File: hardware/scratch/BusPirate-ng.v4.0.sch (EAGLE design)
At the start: 133 parts, among them CON1 CON-USB-F-MICRO-B, IC10 74LVC1G07DBV, IC11 IC_BUFF_SN74LVC1T45DBV, IC12 74LVC1G07DBV, IC13 IC_BUFF_SN74LVC1T45DBV, IC14 74LVC1G07DBV, IC15 IC_BUFF_SN74LVC1T45DBV, IC16 74LVC1G07DBV, IC17 IC_BUFF_SN74LVC1T45DBV, IC2 IC_MEM_23LC1024, IC3 IC_MEM_23LC1024, IC4 IC_74AC573, IC5 IC_BL1551, IC6 IC_BL1551, IC7 74HCT4066PW, IC8 74LVC1G07DBV, IC9 IC_BUFF_SN74LVC1T45DBV, J1 CON_HEADER_1X04, J2 CON_HEADER_1X03-PTH, J3 CON_HEADER_2X02-PTH, J5 CON_HEADER_1X10-RIGHT_ANGLED_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, U1 IC_FPGA_ICE40HX4K, U2 IC_UC_STM32F103ZX, U3 IC_MEM_AT45DB041D

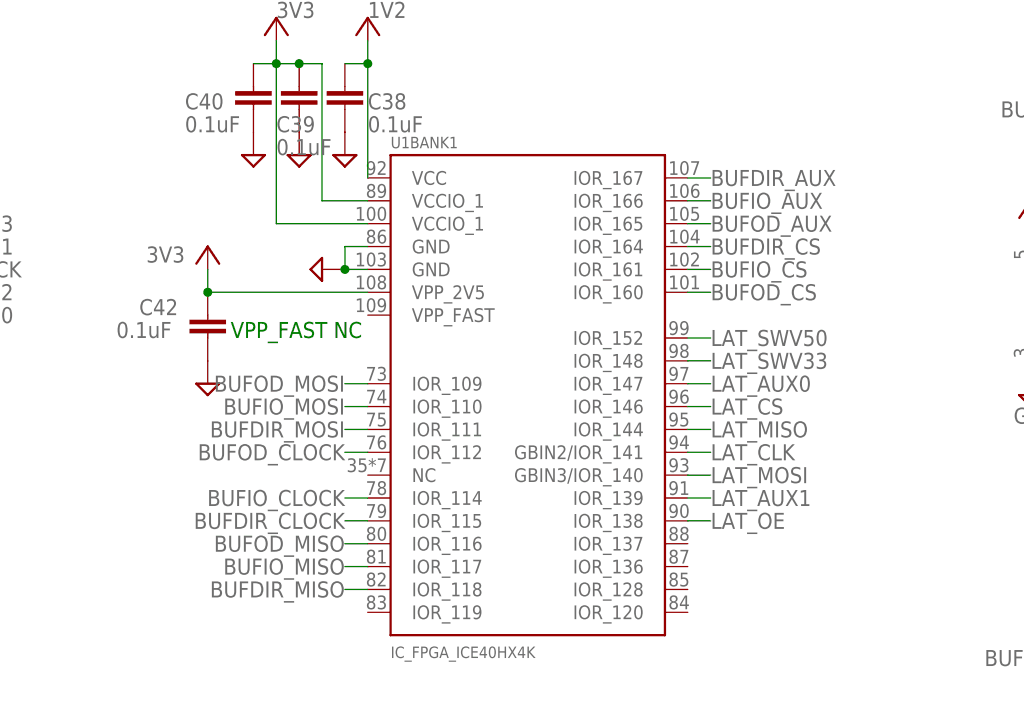
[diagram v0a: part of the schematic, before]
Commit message: Continued routing, swapped some pins on FPGA swapped FPGA pins: BUFOD_CLOCK with BUFOD_MOSI BUFIO_CLOCK with BUFIO_MOSI BUFDIR_CLOCK with BUFDIR_MOSI BUFDIR_AUX with BUFDIR_CS BUFIO_AUX with BUFIO_CS BUFOD_AUX with BUFOD_CS
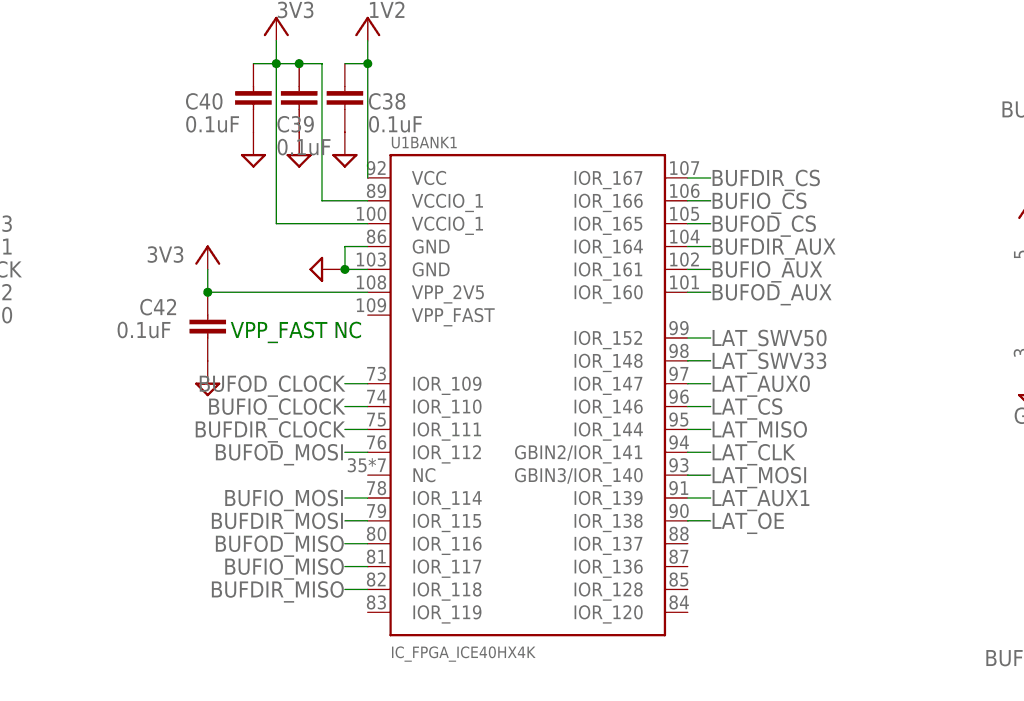
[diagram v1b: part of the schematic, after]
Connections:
- net BUFDIR_AUX: now also U1BANK1.IOR_164; no longer U1BANK1.IOR_167
- net BUFDIR_CLOCK: now also U1BANK1.IOR_111; no longer U1BANK1.IOR_115
- net BUFDIR_CS: now also U1BANK1.IOR_167; no longer U1BANK1.IOR_164
- net BUFDIR_MOSI: now also U1BANK1.IOR_115; no longer U1BANK1.IOR_111
- net BUFIO_AUX: now also U1BANK1.IOR_161; no longer U1BANK1.IOR_166
- net BUFIO_CLOCK: now also U1BANK1.IOR_110; no longer U1BANK1.IOR_114
- net BUFIO_CS: now also U1BANK1.IOR_166; no longer U1BANK1.IOR_161
- net BUFIO_MOSI: now also U1BANK1.IOR_114; no longer U1BANK1.IOR_110
- net BUFOD_AUX: now also U1BANK1.IOR_160; no longer U1BANK1.IOR_165
- net BUFOD_CLOCK: now also U1BANK1.IOR_109; no longer U1BANK1.IOR_112
- net BUFOD_CS: now also U1BANK1.IOR_165; no longer U1BANK1.IOR_160
- net BUFOD_MOSI: now also U1BANK1.IOR_112; no longer U1BANK1.IOR_109
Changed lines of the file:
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@@
 </segment>
 <segment>
-<pinref part="U1" gate="BANK1" pin="IOR_111"/>
-<wire x1="53.34" y1="457.2" x2="50.8" y2="457.2" width="0.1524" layer="91"/>
-<label x="50.8" y="457.2" size="1.778" layer="95" align="center-right"/>
+<pinref part="U1" gate="BANK1" pin="IOR_115"/>
+<wire x1="53.34" y1="447.04" x2="50.8" y2="447.04" width="0.1524" layer="91"/>
+<label x="50.8" y="447.04" size="1.778" layer="95" align="center-right"/>
 </segment>
 </net>
@@
 </segment>
 <segment>
-<pinref part="U1" gate="BANK1" pin="IOR_109"/>
-<wire x1="53.34" y1="462.28" x2="50.8" y2="462.28" width="0.1524" layer="91"/>
-<label x="50.8" y="462.28" size="1.778" layer="95" align="center-right"/>
+<pinref part="U1" gate="BANK1" pin="IOR_112"/>
+<wire x1="53.34" y1="454.66" x2="50.8" y2="454.66" width="0.1524" layer="91"/>
+<label x="50.8" y="454.66" size="1.778" layer="95" align="center-right"/>
 </segment>
 </net>
@@
 </segment>
 <segment>
-<pinref part="U1" gate="BANK1" pin="IOR_110"/>
-<wire x1="53.34" y1="459.74" x2="50.8" y2="459.74" width="0.1524" layer="91"/>
-<label x="50.8" y="459.74" size="1.778" layer="95" align="center-right"/>
+<pinref part="U1" gate="BANK1" pin="IOR_114"/>
+<wire x1="53.34" y1="449.58" x2="50.8" y2="449.58" width="0.1524" layer="91"/>
+<label x="50.8" y="449.58" size="1.778" layer="95" align="center-right"/>
 </segment>
 </net>
@@
 </segment>
 <segment>
-<pinref part="U1" gate="BANK1" pin="IOR_112"/>
-<wire x1="53.34" y1="454.66" x2="50.8" y2="454.66" width="0.1524" layer="91"/>
-<label x="50.8" y="454.66" size="1.778" layer="95" align="center-right"/>
+<pinref part="U1" gate="BANK1" pin="IOR_109"/>
+<wire x1="53.34" y1="462.28" x2="50.8" y2="462.28" width="0.1524" layer="91"/>
+<label x="50.8" y="462.28" size="1.778" layer="95" align="center-right"/>
 </segment>
 </net>
@@
 </segment>
 <segment>
-<pinref part="U1" gate="BANK1" pin="IOR_115"/>
-<wire x1="53.34" y1="447.04" x2="50.8" y2="447.04" width="0.1524" layer="91"/>
-<label x="50.8" y="447.04" size="1.778" layer="95" align="center-right"/>
+<pinref part="U1" gate="BANK1" pin="IOR_111"/>
+<wire x1="53.34" y1="457.2" x2="50.8" y2="457.2" width="0.1524" layer="91"/>
+<label x="50.8" y="457.2" size="1.778" layer="95" align="center-right"/>
 </segment>
 </net>
@@
 </segment>
 <segment>
-<pinref part="U1" gate="BANK1" pin="IOR_114"/>
-<wire x1="53.34" y1="449.58" x2="50.8" y2="449.58" width="0.1524" layer="91"/>
-<label x="50.8" y="449.58" size="1.778" layer="95" align="center-right"/>
+<pinref part="U1" gate="BANK1" pin="IOR_110"/>
+<wire x1="53.34" y1="459.74" x2="50.8" y2="459.74" width="0.1524" layer="91"/>
+<label x="50.8" y="459.74" size="1.778" layer="95" align="center-right"/>
 </segment>
 </net>
@@
 </segment>
 <segment>
-<pinref part="U1" gate="BANK1" pin="IOR_161"/>
-<wire x1="88.9" y1="474.98" x2="91.44" y2="474.98" width="0.1524" layer="91"/>
-<label x="91.44" y="474.98" size="1.778" layer="95" align="center-left"/>
+<pinref part="U1" gate="BANK1" pin="IOR_166"/>
+<wire x1="88.9" y1="482.6" x2="91.44" y2="482.6" width="0.1524" layer="91"/>
+<label x="91.44" y="482.6" size="1.778" layer="95" align="center-left"/>
 </segment>
 </net>
@@
 </segment>
 <segment>
-<pinref part="U1" gate="BANK1" pin="IOR_164"/>
-<wire x1="88.9" y1="477.52" x2="91.44" y2="477.52" width="0.1524" layer="91"/>
-<label x="91.44" y="477.52" size="1.778" layer="95" align="center-left"/>
+<pinref part="U1" gate="BANK1" pin="IOR_167"/>
+<wire x1="88.9" y1="485.14" x2="91.44" y2="485.14" width="0.1524" layer="91"/>
+<label x="91.44" y="485.14" size="1.778" layer="95" align="center-left"/>
 </segment>
 </net>
@@
 </segment>
 <segment>
-<pinref part="U1" gate="BANK1" pin="IOR_160"/>
-<wire x1="88.9" y1="472.44" x2="91.44" y2="472.44" width="0.1524" layer="91"/>
-<label x="91.44" y="472.44" size="1.778" layer="95" align="center-left"/>
+<pinref part="U1" gate="BANK1" pin="IOR_165"/>
+<wire x1="88.9" y1="480.06" x2="91.44" y2="480.06" width="0.1524" layer="91"/>
+<label x="91.44" y="480.06" size="1.778" layer="95" align="center-left"/>
 </segment>
 </net>
@@
 </segment>
 <segment>
-<pinref part="U1" gate="BANK1" pin="IOR_166"/>
-<wire x1="88.9" y1="482.6" x2="91.44" y2="482.6" width="0.1524" layer="91"/>
-<label x="91.44" y="482.6" size="1.778" layer="95" align="center-left"/>
+<pinref part="U1" gate="BANK1" pin="IOR_161"/>
+<wire x1="88.9" y1="474.98" x2="91.44" y2="474.98" width="0.1524" layer="91"/>
+<label x="91.44" y="474.98" size="1.778" layer="95" align="center-left"/>
 </segment>
 </net>
@@
 </segment>
 <segment>
-<pinref part="U1" gate="BANK1" pin="IOR_167"/>
-<wire x1="88.9" y1="485.14" x2="91.44" y2="485.14" width="0.1524" layer="91"/>
-<label x="91.44" y="485.14" size="1.778" layer="95" align="center-left"/>
+<pinref part="U1" gate="BANK1" pin="IOR_164"/>
+<wire x1="88.9" y1="477.52" x2="91.44" y2="477.52" width="0.1524" layer="91"/>
+<label x="91.44" y="477.52" size="1.778" layer="95" align="center-left"/>
 </segment>
 </net>
@@
 </segment>
 <segment>
-<pinref part="U1" gate="BANK1" pin="IOR_165"/>
-<wire x1="88.9" y1="480.06" x2="91.44" y2="480.06" width="0.1524" layer="91"/>
-<label x="91.44" y="480.06" size="1.778" layer="95" align="center-left"/>
-</segment>
-</net>
+<pinref part="U1" gate="BANK1" pin="IOR_160"/>
+<wire x1="88.9" y1="472.44" x2="91.44" y2="472.44" width="0.1524" layer="91"/>
+<label x="91.44" y="472.44" size="1.778" layer="95" align="center-left"/>
+</segment>
+</net>

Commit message: move some pins, wire vrefs, change caps size and continue routing -wire vref+ and vref- to 3.3V and GND -wired MCU_INT0 to PE2 and MCU_INT1 to PE3, to have each pin a dedicated interrupt. -change capacitor size from 0604 to 0402 capacitors C20, C45 and C47 -moved USB_DET from PF11 to PE4
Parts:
- removed C28: 0.1uF, rcl:C-EUC0603
- added C20: 0.1uF, dp_devices.v6:CAPACITOR_NPOL-0402
- C45, C47: device rcl:C-EUC0603 -> dp_devices.v6:CAPACITOR_NPOL-0402
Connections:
- removed net N$27: U2U.PE2/FT/FSMC_A23
- net 1V2: now also C20.1; no longer C45.2
- net 3V3: now also C45.1, C47.1, U2U.VREF+; no longer C28.2, C47.2
- net GND: now also C20.2, C45.2, C47.2, U2U.VREF-; no longer C28.1, C45.1, C47.1
- net MCU_INT0: now also U2U.PE2/FT/FSMC_A23; no longer U2U.UART4_RX/USART3_RX('01')/FT/PC11
- net MCU_INT1: now also U2U.PE3/FT/FSMC_A19; no longer U2U.UART4_TX/USART3_TX('01')/FT/PC10
- net USB_DET: now also U2U.PE4/FT/FSMC_A20; no longer U2U.FSMC_NIOS16/FT/PF11
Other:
- moved on the sheet: C46, R40

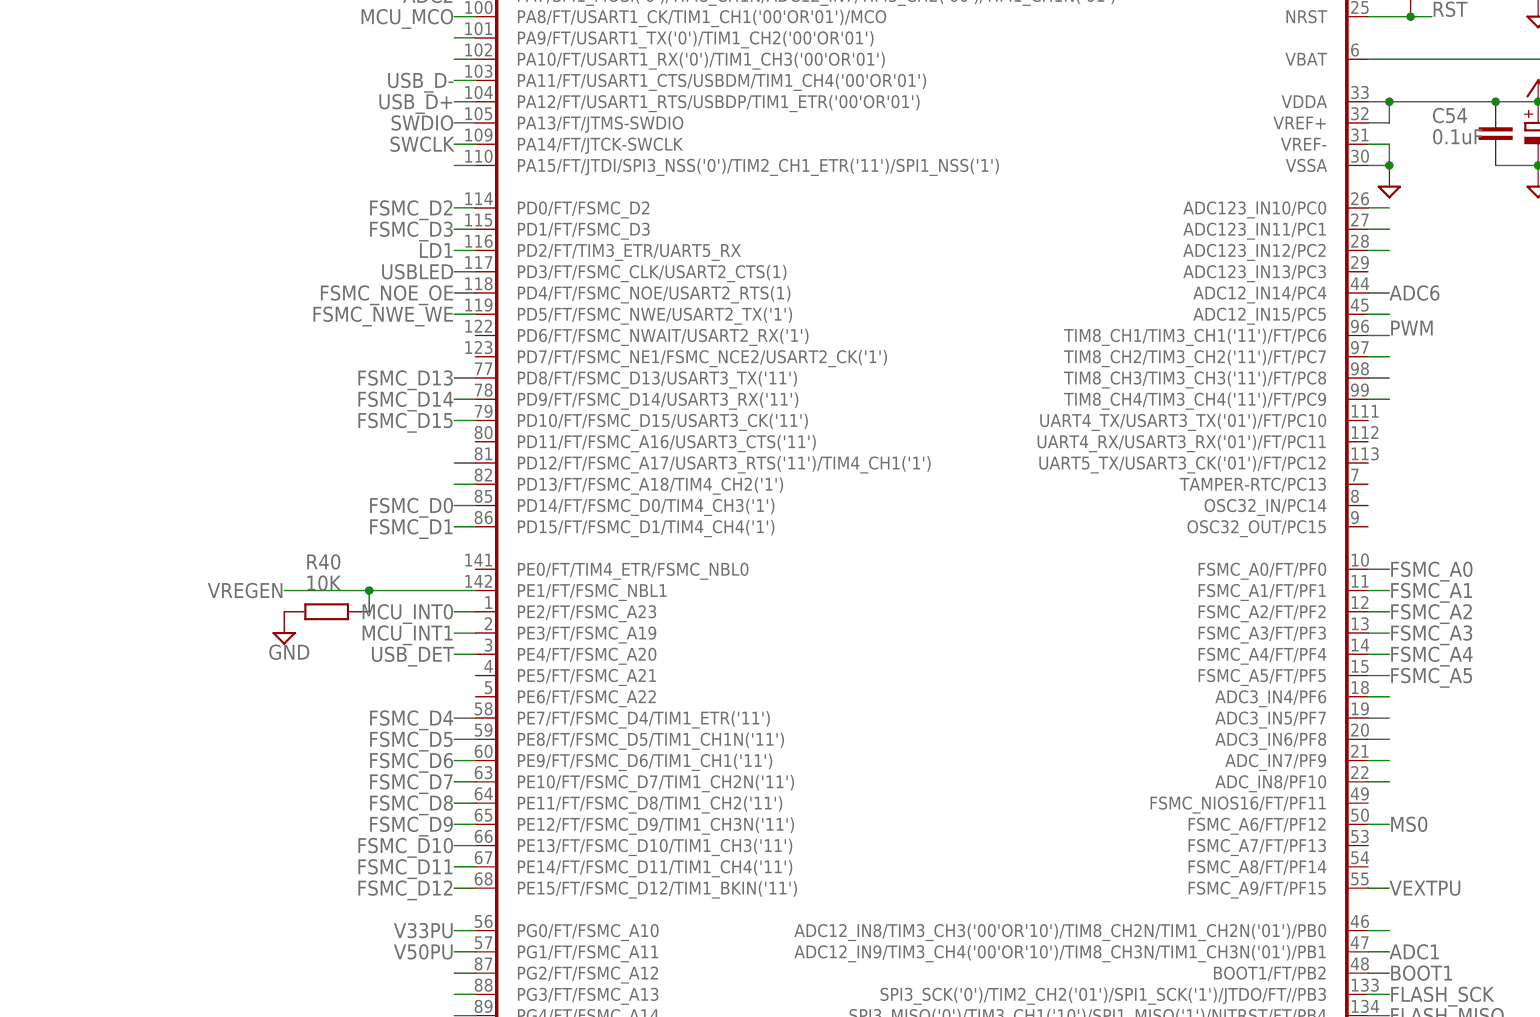
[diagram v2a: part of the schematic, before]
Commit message: moving some pins and continue routing -move VREGEN from MCU pin PE1 to PD2 -move LD1 from MCU PD2 to PA15
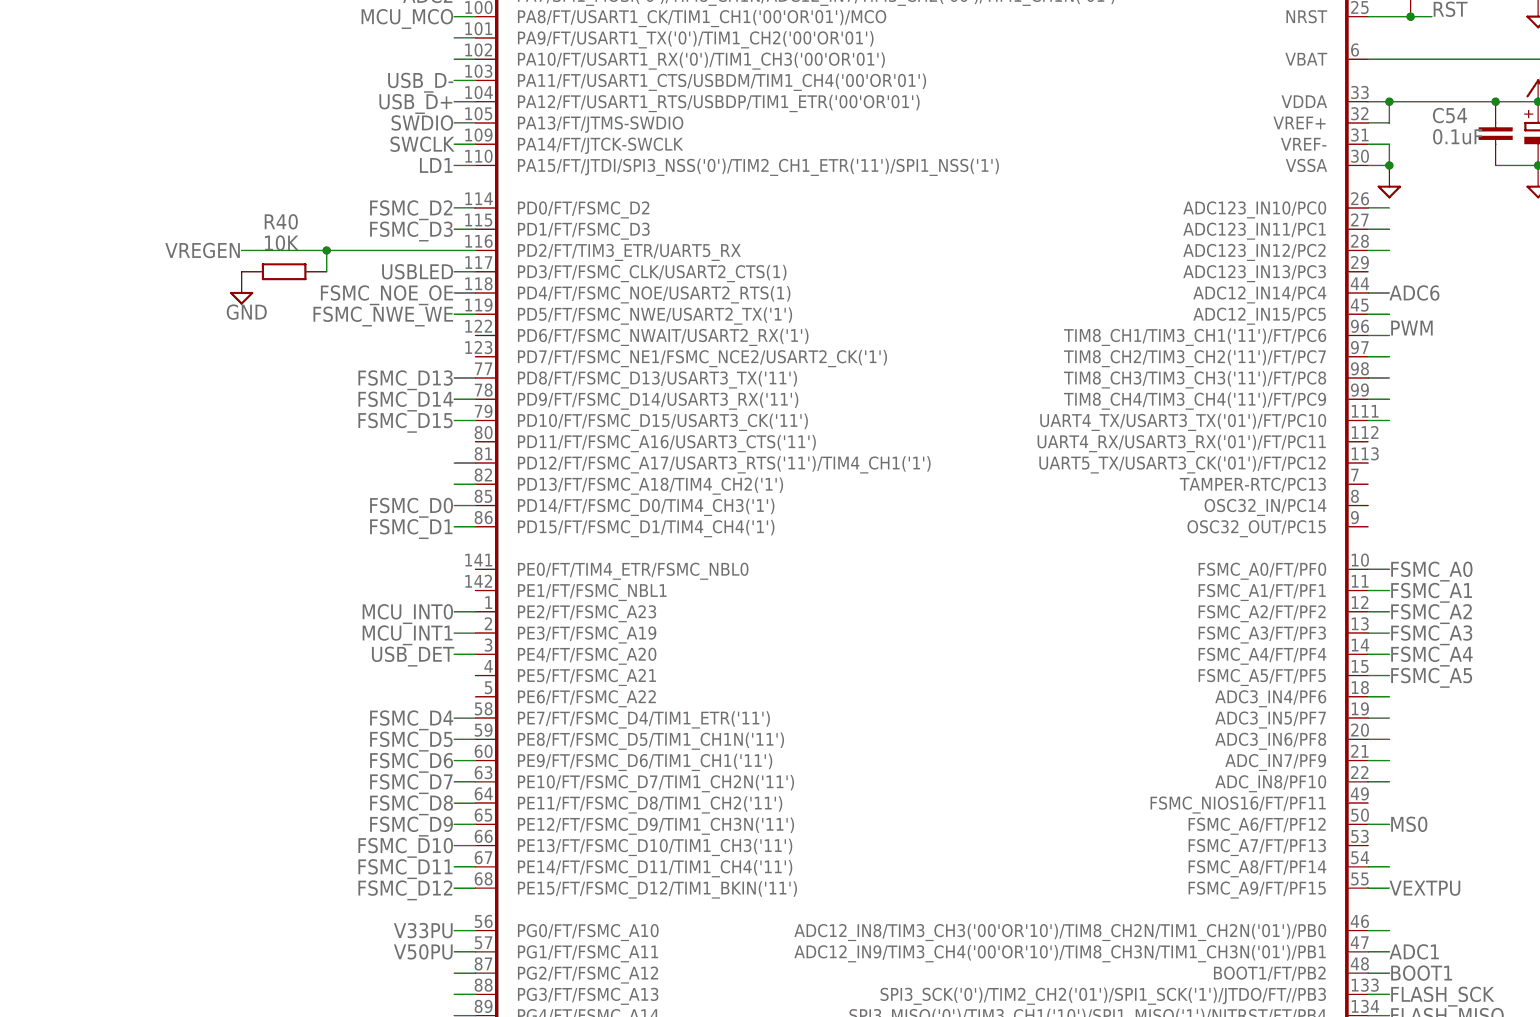
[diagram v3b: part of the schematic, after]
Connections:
- removed net N$47: U2U.PA15/FT/JTDI/SPI3_NSS('0')/TIM2_CH1_ETR('11')/SPI1_NSS('1')
- new net N$15: U2U.FSMC_A8/FT/PF14
- net LD1: now also U2U.PA15/FT/JTDI/SPI3_NSS('0')/TIM2_CH1_ETR('11')/SPI1_NSS('1'); no longer U2U.PD2/FT/TIM3_ETR/UART5_RX
- net USBLED: now also U2U.UART4_TX/USART3_TX('01')/FT/PC10
- net VREGEN: now also U2U.PD2/FT/TIM3_ETR/UART5_RX; no longer U2U.PE1/FT/FSMC_NBL1
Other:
- moved on the sheet: R40
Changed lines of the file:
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@@
 <instance part="SUPPLY100" gate="GND" x="-121.92" y="149.86" smashed="yes"/>
 <instance part="SUPPLY101" gate="GND" x="-139.7" y="149.86" smashed="yes"/>
-<instance part="R40" gate="G$1" x="-266.7" y="99.06" smashed="yes" rot="R180">
-<attribute name="NAME" x="-269.24" y="104.14" size="1.778" layer="95"/>
-<attribute name="VALUE" x="-269.24" y="101.6" size="1.778" layer="96"/>
+<instance part="R40" gate="G$1" x="-271.78" y="139.7" smashed="yes" rot="R180">
+<attribute name="NAME" x="-274.32" y="144.78" size="1.778" layer="95"/>
+<attribute name="VALUE" x="-274.32" y="142.24" size="1.778" layer="96"/>
 </instance>
-<instance part="SUPPLY102" gate="GND" x="-271.78" y="96.52"/>
+<instance part="SUPPLY102" gate="GND" x="-276.86" y="137.16"/>
 <instance part="J5" gate="J" x="243.84" y="304.8" rot="MR180"/>
 <instance part="C55" gate="G$1" x="35.56" y="373.38" smashed="yes" rot="R180">
@@
 </segment>
 <segment>
-<pinref part="U2" gate="U" pin="PD2/FT/TIM3_ETR/UART5_RX"/>
-<wire x1="-248.92" y1="142.24" x2="-251.46" y2="142.24" width="0.1524" layer="91"/>
-<label x="-251.46" y="142.24" size="1.778" layer="95" align="center-right"/>
+<pinref part="U2" gate="U" pin="PA15/FT/JTDI/SPI3_NSS('0')/TIM2_CH1_ETR('11')/SPI1_NSS('1')"/>
+<wire x1="-248.92" y1="152.4" x2="-251.46" y2="152.4" width="0.1524" layer="91"/>
+<label x="-251.46" y="152.4" size="1.778" layer="95" align="center-right"/>
 </segment>
 </net>
@@
 </segment>
 <segment>
-<pinref part="U2" gate="U" pin="PE1/FT/FSMC_NBL1"/>
-<label x="-271.78" y="101.6" size="1.778" layer="95" align="center-right"/>
+<label x="-276.86" y="142.24" size="1.778" layer="95" align="center-right"/>
 <pinref part="R40" gate="G$1" pin="1"/>
-<wire x1="-248.92" y1="101.6" x2="-261.62" y2="101.6" width="0.1524" layer="91"/>
-<wire x1="-261.62" y1="101.6" x2="-271.78" y2="101.6" width="0.1524" layer="91"/>
-<wire x1="-261.62" y1="99.06" x2="-261.62" y2="101.6" width="0.1524" layer="91"/>
-<junction x="-261.62" y="101.6"/>
+<wire x1="-266.7" y1="142.24" x2="-276.86" y2="142.24" width="0.1524" layer="91"/>
+<wire x1="-266.7" y1="139.7" x2="-266.7" y2="142.24" width="0.1524" layer="91"/>
+<pinref part="U2" gate="U" pin="PD2/FT/TIM3_ETR/UART5_RX"/>
+<wire x1="-266.7" y1="142.24" x2="-248.92" y2="142.24" width="0.1524" layer="91"/>
+<junction x="-266.7" y="142.24"/>
 </segment>
 </net>
@@
 <label x="-251.46" y="139.7" size="1.778" layer="95" align="center-right"/>
 </segment>
+<segment>
+<pinref part="U2" gate="U" pin="UART4_TX/USART3_TX('01')/FT/PC10"/>
+<wire x1="-142.24" y1="121.92" x2="-139.7" y2="121.92" width="0.1524" layer="91"/>
+</segment>
 </net>
 <net name="RST" class="0">
@@
 </segment>
 </net>
-<net name="N$47" class="0">
-<segment>
-<pinref part="U2" gate="U" pin="PA15/FT/JTDI/SPI3_NSS('0')/TIM2_CH1_ETR('11')/SPI1_NSS('1')"/>
-<wire x1="-248.92" y1="152.4" x2="-251.46" y2="152.4" width="0.1524" layer="91"/>
-</segment>
-</net>
 <net name="N$50" class="0">
 <segment>
@@
 </segment>
 </net>
+<net name="N$15" class="0">
+<segment>
+<pinref part="U2" gate="U" pin="FSMC_A8/FT/PF14"/>
+<wire x1="-142.24" y1="68.58" x2="-139.7" y2="68.58" width="0.1524" layer="91"/>
+</segment>
+</net>
